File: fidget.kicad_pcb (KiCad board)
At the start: 2 copper layers, 13 parts, among them SW1 SW_Push, SW2 SW_Push, SW3 SW_Push, SW4 SW_Push, U1 XIAO-RP2040-DIP

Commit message: add xiao 3d model
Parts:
- D1, D2, D3, D4: footprint general:LEDRD254W57D500H1070 -> general:LEDRD254W57D500H1070_3d
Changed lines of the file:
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@@
 		)
 	)
-	(footprint "general:LEDRD254W57D500H1070"
+	(footprint "general:LEDRD254W57D500H1070_3d"
 		(layer "F.Cu")
 		(at 146.23125 76.2)
@@
 			)
 		)
-		(property "Footprint" "general:LEDRD254W57D500H1070"
+		(property "Footprint" "general:LEDRD254W57D500H1070_3d"
 			(at 0 0 0)
 			(layer "F.Fab")
@@
 			(solder_mask_margin 0.102)
 		)
+		(model "${KIPRJMOD}/3d/led.STEP"
+			(offset
+				(xyz 0 0 0)
+			)
+			(scale
+				(xyz 1 1 1)
+			)
+			(rotate
+				(xyz -90 0 0)
+			)
+		)
 	)
-	(footprint "general:LEDRD254W57D500H1070"
+	(footprint "general:LEDRD254W57D500H1070_3d"
 		(layer "F.Cu")
 		(at 139 76.2)
@@
 			)
 		)
-		(property "Footprint" "general:LEDRD254W57D500H1070"
+		(property "Footprint" "general:LEDRD254W57D500H1070_3d"
 			(at 0 0 0)
 			(layer "F.Fab")
@@
 			(pintype "passive")
 			(solder_mask_margin 0.102)
+		)
+		(model "${KIPRJMOD}/3d/led.STEP"
+			(offset
+				(xyz 0 0 0)
+			)
+			(scale
+				(xyz 1 1 1)
+			)
+			(rotate
+				(xyz -90 0 0)
+			)
 		)
 	)
@@
 		)
 		(model "${AMZPATH}/3dmodels/AMz3D.3dshapes/Seeeduino XIAO SAMD21 v4.step"
+			(hide yes)
 			(offset
 				(xyz 0 0 0)
@@
 			(rotate
 				(xyz -90 0 0)
+			)
+		)
+		(model "${KIPRJMOD}/3d/xiao_rp2040_v26.step"
+			(offset
+				(xyz 0 0 0)
+			)
+			(scale
+				(xyz 1 1 1)
+			)
+			(rotate
+				(xyz 0 0 0)
 			)
 		)
@@
 		)
 	)
-	(footprint "general:LEDRD254W57D500H1070"
+	(footprint "general:LEDRD254W57D500H1070_3d"
 		(layer "F.Cu")
 		(at 139.13 85)
@@
 			)
 		)
-		(property "Footprint" "general:LEDRD254W57D500H1070"
+		(property "Footprint" "general:LEDRD254W57D500H1070_3d"
 			(at 0 0 0)
 			(layer "F.Fab")
@@
 			(pintype "passive")
 			(solder_mask_margin 0.102)
+		)
+		(model "${KIPRJMOD}/3d/led.STEP"
+			(offset
+				(xyz 0 0 0)
+			)
+			(scale
+				(xyz 1 1 1)
+			)
+			(rotate
+				(xyz -90 0 0)
+			)
 		)
 	)
@@
 		)
 	)
-	(footprint "general:LEDRD254W57D500H1070"
+	(footprint "general:LEDRD254W57D500H1070_3d"
 		(layer "F.Cu")
 		(at 146.5 85)
@@
 			)
 		)
-		(property "Footprint" "general:LEDRD254W57D500H1070"
+		(property "Footprint" "general:LEDRD254W57D500H1070_3d"
 			(at 0 0 0)
 			(layer "F.Fab")
@@
 			(solder_mask_margin 0.102)
 		)
+		(model "${KIPRJMOD}/3d/led.STEP"
+			(offset
+				(xyz 0 0 0)
+			)
+			(scale
+				(xyz 1 1 1)
+			)
+			(rotate
+				(xyz -90 0 0)
+			)
+		)
 	)

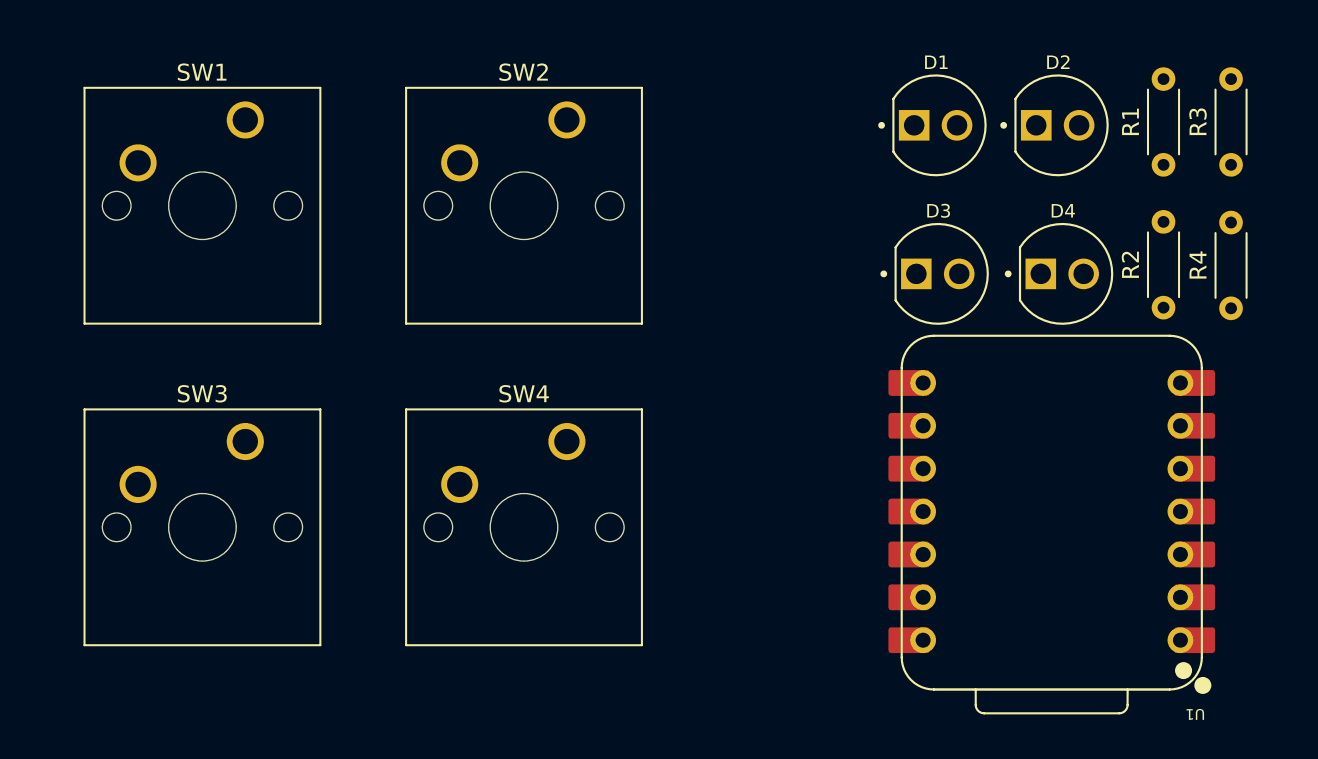
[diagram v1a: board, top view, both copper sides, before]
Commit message: routing + ground plane
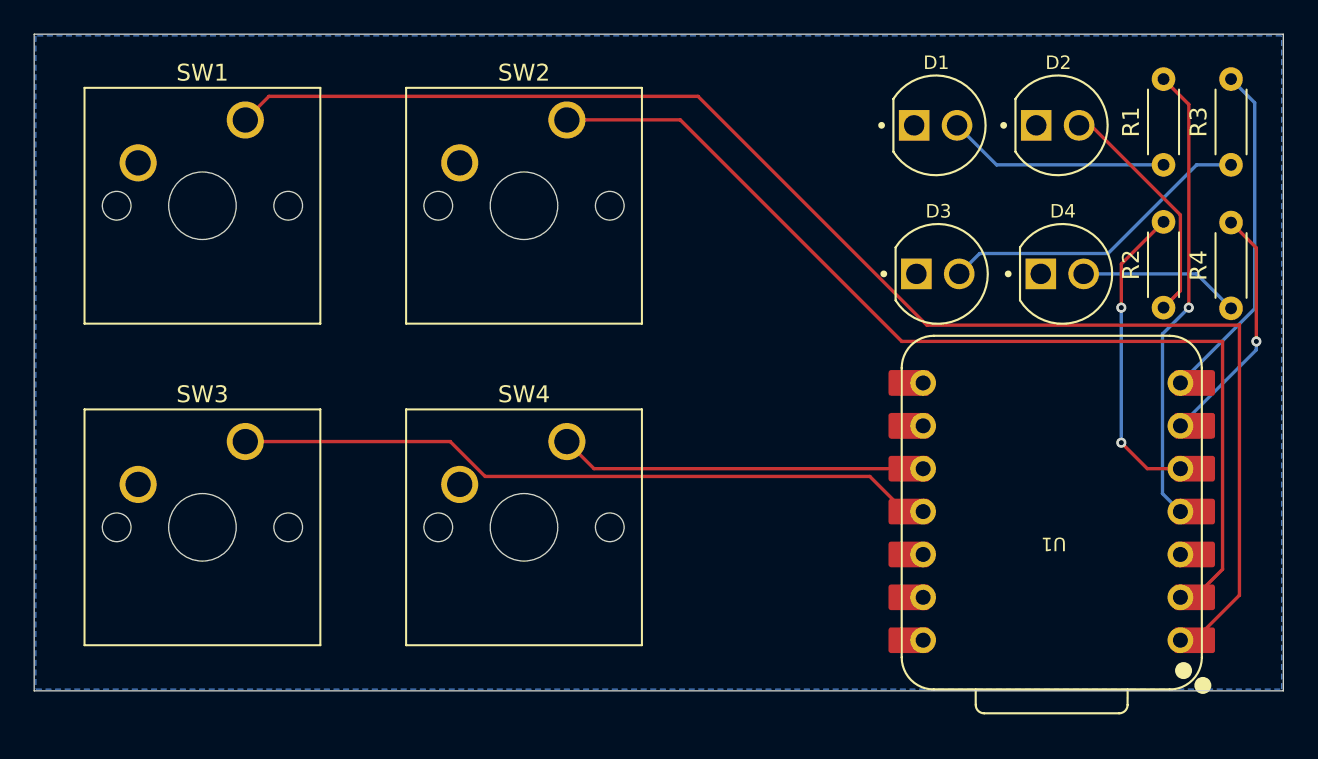
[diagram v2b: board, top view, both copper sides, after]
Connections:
- U1 pad 10: unconnected-(U1-GPIO4/MISO-Pad10)_1 -> button4
- U1 pad 11: unconnected-(U1-GPIO3/MOSI-Pad11) -> button3
- U1 pad 3: button3 -> unconnected-(U1-GPIO28/ADC2/A2-Pad3)_1
- U1 pad 6: led3 -> led4
- U1 pad 7: unconnected-(U1-GPIO0/TX-Pad7) -> led3
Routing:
- net button1: track 0.00 -> 84.9 mm
- net button2: track 0.00 -> 60.1 mm
- net button3: track 0.00 -> 41.9 mm
- net led1: track 0.00 -> 27.3 mm, vias 0 -> 1
- net button4: track 0.00 -> 21.8 mm
- net led3: track 0.00 -> 20.4 mm
- net Net-(D3-PadA): track 0.00 -> 18.8 mm
- net led2: track 0.00 -> 18.3 mm, vias 0 -> 2
- net led4: track 0.00 -> 14.5 mm, vias 0 -> 1
- net Net-(D2-PadA): track 0.00 -> 14.1 mm
- net Net-(D1-PadA): track 0.00 -> 13.2 mm
- net Net-(D4-PadA): track 0.00 -> 9.58 mm
- added copper zone on B.Cu, net GND
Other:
- board outline added: 74 x 38.9 mm
